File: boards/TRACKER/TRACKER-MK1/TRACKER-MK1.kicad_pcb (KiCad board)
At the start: 2 copper layers, 76.2 x 152.4 mm, 120 parts, among them J101 1054500101, J102 JST-PH, J103 1040310811, J104 JST-PH, J105 JST-PH, J106 JST-PH, J107 JST-PH, J108 JST-PH, J109 JST-PH, J110 U.FL, J111 2.54mm Pin Header, J112 2.54mm Pin Header, J113 2.54mm Pin Header, J114 2.54mm Pin Header, J115 2.54mm Pin Header, J116 2.54mm Pin Header, J117 2.54mm Pin Header, J118 2.54mm Pin Header, J119 2.54mm Pin Header, J120 2.54mm Pin Header, SW101 VBUS Switch, SW102 Battery Switch, SW103 Power Switch, SW104 SW_Push, SW105 SW_Push, U101 BQ25180, U102 ECMF02-2AMX6, U103 ADS7138-Q1, U104 ADS7138-Q1, U105 TPS566242DRLR, U106 ESP32-S3-WROOM-1, U107 BNO085, U108 SAM-M10Q-00B, U201 CC1125, X201 ECS-TXO-2016MV-400-TR

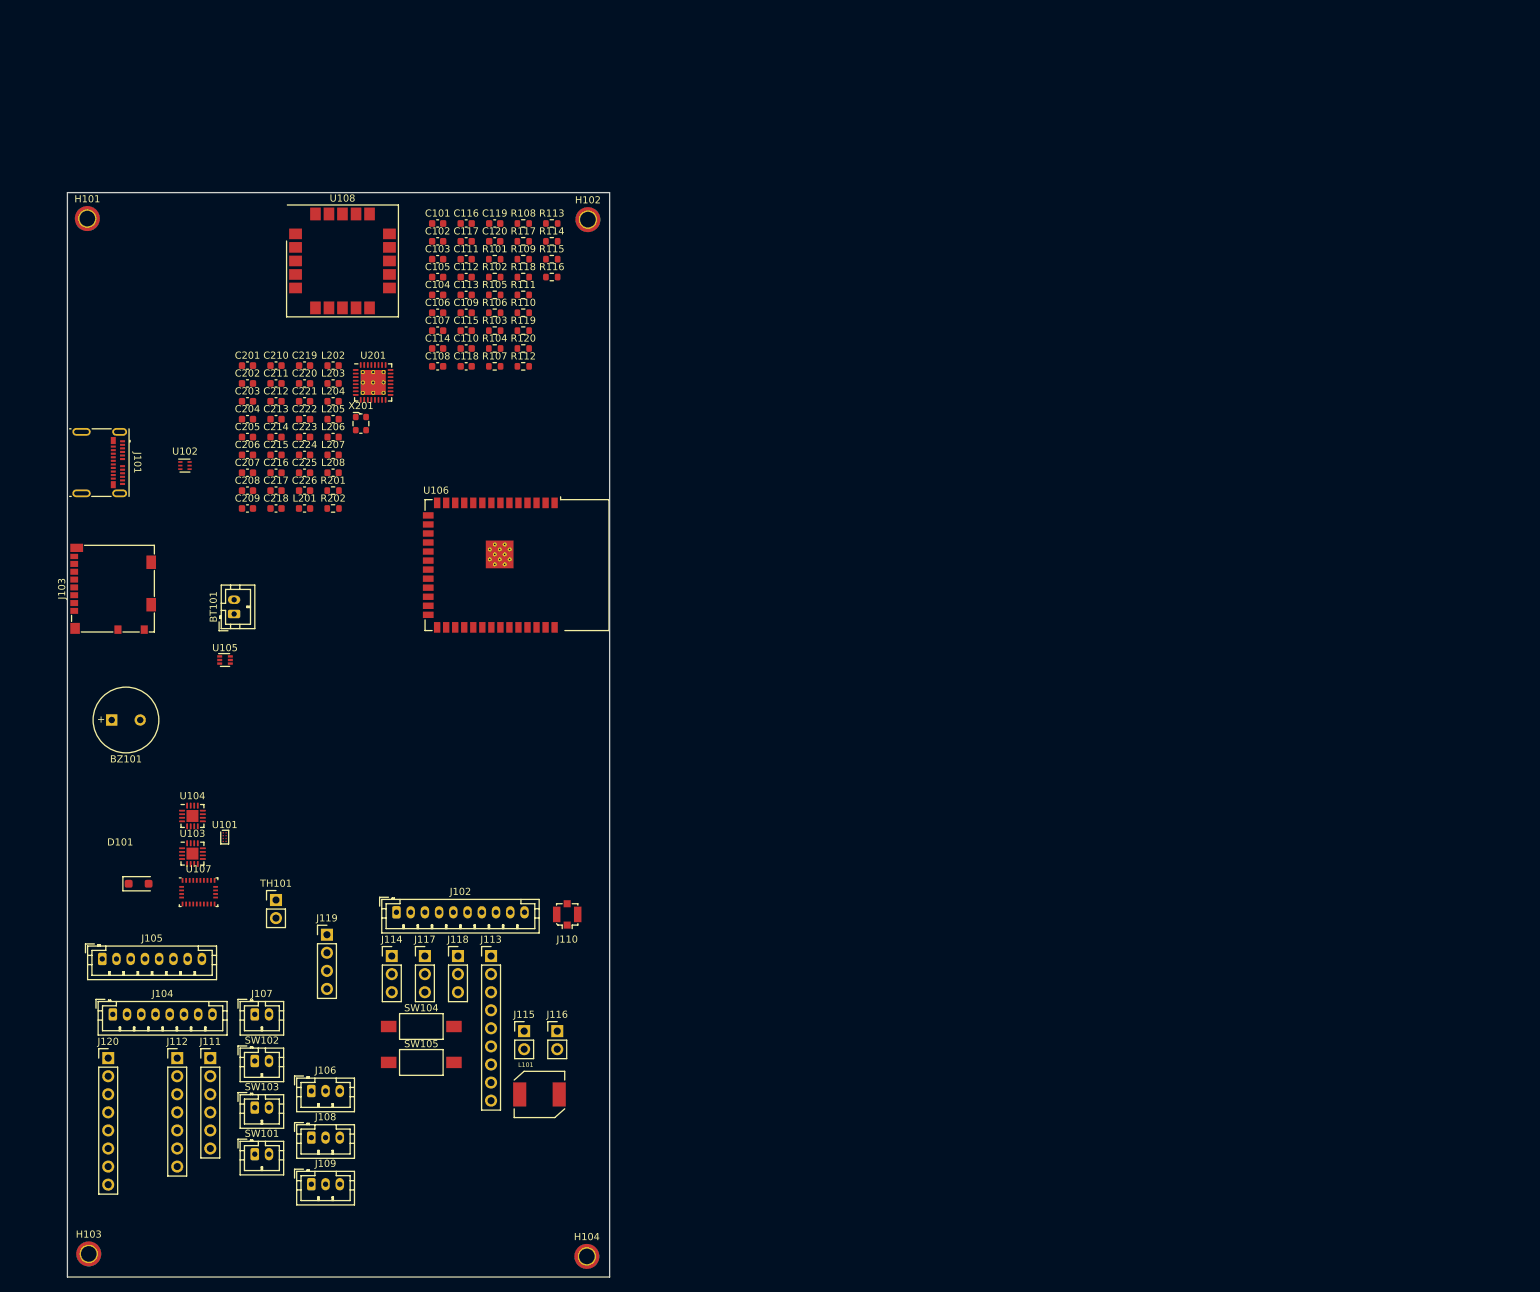
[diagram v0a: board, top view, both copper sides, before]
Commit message: Added GPIO expanders, Done schematic
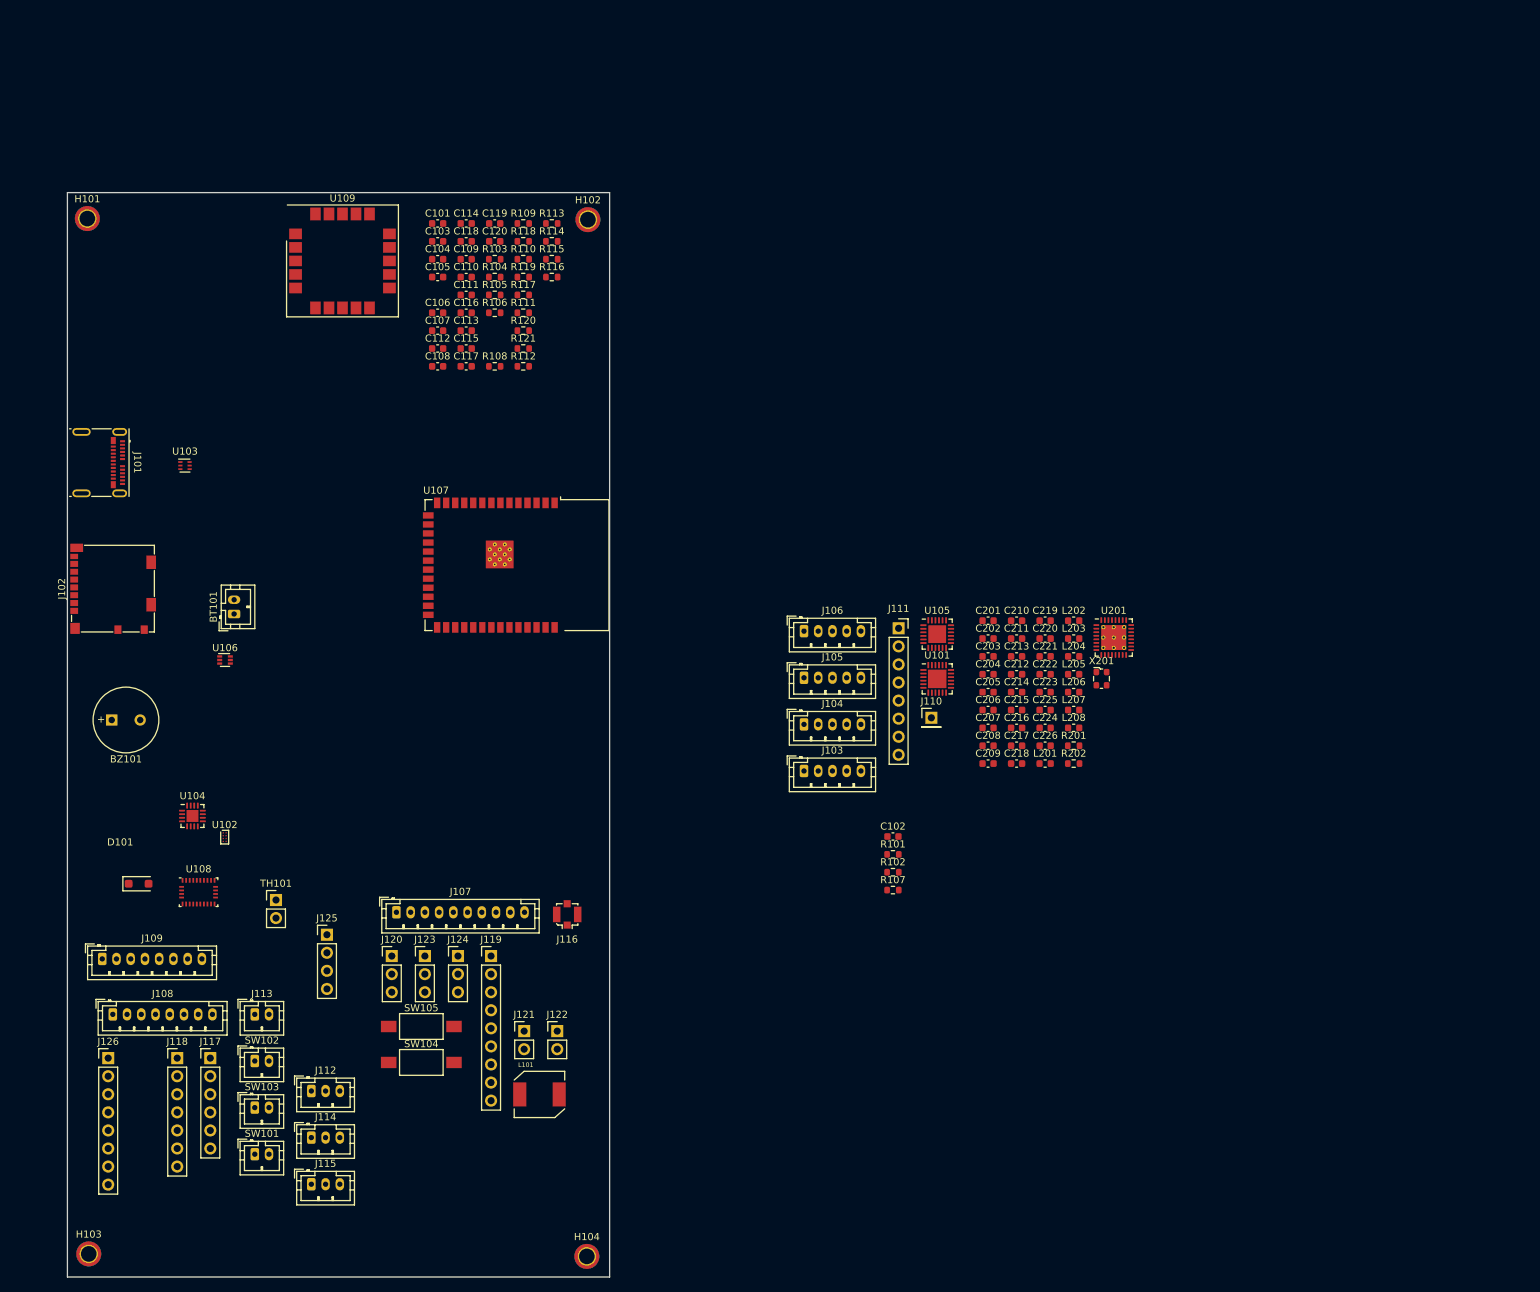
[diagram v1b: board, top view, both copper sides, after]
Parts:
- removed the C104 at (128.2, 39.8)
- removed the R103 at (136.3, 44.8)
- removed the R104 at (136.3, 47.3)
- removed the U103 at (93.8, 118.3)
- added C102: 0.1uF, Capacitor_SMD:C_0603_1608Metric, F.Cu at (192.2, 115.9)
- added J103: JST-PH, Connector_JST:JST_PH_B5B-PH-K_1x05_P2.00mm_Vertical, F.Cu at (179.7, 106.7)
- added J104: JST-PH, Connector_JST:JST_PH_B5B-PH-K_1x05_P2.00mm_Vertical, F.Cu at (179.7, 100.1)
- added J105: JST-PH, Connector_JST:JST_PH_B5B-PH-K_1x05_P2.00mm_Vertical, F.Cu at (179.7, 93.6)
- added J106: JST-PH, Connector_JST:JST_PH_B5B-PH-K_1x05_P2.00mm_Vertical, F.Cu at (179.7, 87.0)
- added J110: 2.54mm Pin Header, Connector_PinHeader_2.54mm:PinHeader_1x01_P2.54mm_Vertical, F.Cu at (197.6, 99.2)
- added J111: 2.54mm Pin Header, Connector_PinSocket_2.54mm:PinSocket_1x08_P2.54mm_Vertical, F.Cu at (193.0, 86.6)
- added R101: 10k, Resistor_SMD:R_0603_1608Metric, F.Cu at (192.2, 118.4)
- added R102: 10k, Resistor_SMD:R_0603_1608Metric, F.Cu at (192.2, 120.9)
- added R107: 10k, Resistor_SMD:R_0603_1608Metric, F.Cu at (192.2, 123.4)
- added U101: TCAL9539-Q1, Package_DFN_QFN:WQFN-24-1EP_4x4mm_P0.5mm_EP2.6x2.6mm, F.Cu at (198.4, 93.7)
- added U105: ADP5589, Package_CSP:LFCSP-24-1EP_4x4mm_P0.5mm_EP2.5x2.5mm, F.Cu at (198.4, 87.5)
- C205: value 47nF -> 33pF
- C206: value 220nF -> 100pF
- C207: value 47nF -> 15pF
- C209: value 33pF -> 220nF
- C210: value 100pF -> 47nF
- C211: value 10nF -> 47nF
- C212: value 47nF -> 3.3pF
- C213: value 47nF -> 1pF
- C214: value 3.3pF -> 47nF
- C215: value 15pF -> 47nF
- C216: value 47nF -> 2.2pF
- C217: value 3.3pF -> 10nF
- C219: value 1pF -> 47nF
- C221: value 47nF -> 3pF
- C222: value 2.2pF -> 3.3pF
- C225: value 3pF -> TBD
- C226: value C -> 47nF
- L202: value 15nH -> 12nH
- L203: value 12nH -> 7.5nH
- L204: value 12nH -> 15nH
- L205: value 7.5nH -> 12nH
- L206: value 12nH -> 18nH
- L207: value 18nH -> 12nH
- moved C212 110.9 mm to (209.6, 93.1)
- moved C224 110.9 mm to (213.6, 100.6)
- moved C207 110.1 mm to (205.6, 100.6)
- moved L208 110.1 mm to (217.6, 100.6)
- moved C210 110.1 mm to (209.6, 85.6)
- moved C215 110.1 mm to (209.6, 98.1)
- moved C216 110.1 mm to (209.6, 100.6)
- moved U201 110.1 mm to (223.2, 87.9)
- moved C201 110.1 mm to (205.6, 85.6)
- moved C202 110.1 mm to (205.6, 88.1)
- moved C203 110.1 mm to (205.6, 90.6)
- moved C204 110.1 mm to (205.6, 93.1)
- moved C205 110.1 mm to (205.6, 95.6)
- moved C206 110.1 mm to (205.6, 98.1)
- moved C208 110.1 mm to (205.6, 103.1)
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- renumbered C102 to C103, C103 to C104, C111 to C109, C112 to C110, C113 to C111, C114 to C112, C115 to C113, C116 to C114, C110 to C115, C109 to C116, C118 to C117, C117 to C118, J103 to J102, J102 to J107, J104 to J108, J105 to J109, J106 to J112, J107 to J113, J108 to J114, J109 to J115, J110 to J116, J111 to J117, J112 to J118, J113 to J119, J114 to J120, J115 to J121, J116 to J122, J117 to J123, J118 to J124, J119 to J125, J120 to J126, R101 to R103, R102 to R104, R107 to R108, R108 to R109, R109 to R110, R110 to R111, R111 to R117, R117 to R118, R118 to R119, R119 to R120, R120 to R121, SW105 to SW104, SW104 to SW105, U101 to U102, U102 to U103, U105 to U106, U106 to U107, U107 to U108, U108 to U109
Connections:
- C204 pad 1: Net-(C204-Pad1) -> /3V3
- C205 pad 1: /3V3 -> Net-(C205-Pad1)
- C205 pad 2: GND -> /3V3
- C206 pad 1: Net-(U201-DCPL) -> /3V3
- C207 pad 1: Net-(U201-DCPL_PFD_CHP) -> Net-(U201-PA)
- C207 pad 2: GND -> Net-(C207-Pad2)
- C209 pad 1: Net-(C209-Pad1) -> Net-(U201-DCPL)
- C209 pad 2: Net-(C204-Pad1) -> GND
- C210 pad 1: Net-(C204-Pad1) -> Net-(U201-DCPL_PFD_CHP)
- C211 pad 1: Net-(U201-DCPL_VCO) -> /3V3
- C212 pad 1: /Radio/DCPL_XOSC -> Net-(C212-Pad1)
- C212 pad 2: GND -> Net-(U201-LNA_N)
- C213 pad 1: /3V3 -> Net-(C207-Pad2)
- C213 pad 2: GND -> Net-(C213-Pad2)
- C214 pad 1: Net-(C214-Pad1) -> /3V3
- C214 pad 2: Net-(U201-LNA_N) -> GND
- C215 pad 1: Net-(U201-PA) -> /3V3
- C215 pad 2: Net-(C215-Pad2) -> GND
- C216 pad 1: /3V3 -> Net-(C213-Pad2)
- C216 pad 2: GND -> Net-(U201-TRX_SW)
- C217 pad 1: GND -> Net-(U201-DCPL_VCO)
- C217 pad 2: Net-(U201-LNA_P) -> GND
- C218 pad 1: /3V3 -> Net-(U201-DCPL_XOSC)
- C219 pad 1: Net-(C215-Pad2) -> /3V3
- C219 pad 2: Net-(C219-Pad2) -> GND
- C221 pad 1: /3V3 -> GND
- C221 pad 2: GND -> Net-(C221-Pad2)
- C222 pad 1: Net-(C219-Pad2) -> GND
- C222 pad 2: Net-(U201-TRX_SW) -> Net-(U201-LNA_P)
- C225 pad 1: GND -> Net-(C221-Pad2)
- C225 pad 2: Net-(C225-Pad2) -> /Radio/ANT
- C226 pad 1: Net-(C225-Pad2) -> /3V3
- C226 pad 2: /Radio/ANT -> GND
- L201 pad 2: Net-(C209-Pad1) -> Net-(C205-Pad1)
- L202 pad 1: Net-(U201-LNA_P) -> GND
- L203 pad 1: Net-(U201-LNA_P) -> Net-(C207-Pad2)
- L203 pad 2: Net-(C214-Pad1) -> Net-(C213-Pad2)
- L204 pad 2: GND -> Net-(U201-LNA_P)
- L205 pad 1: Net-(C215-Pad2) -> Net-(U201-TRX_SW)
- L205 pad 2: Net-(C219-Pad2) -> Net-(C212-Pad1)
- L206 pad 1: Net-(C214-Pad1) -> Net-(C213-Pad2)
- L206 pad 2: Net-(U201-TRX_SW) -> Net-(C221-Pad2)
- L207 pad 1: Net-(C219-Pad2) -> Net-(C212-Pad1)
- L207 pad 2: Net-(C225-Pad2) -> Net-(U201-LNA_P)
- L208 pad 1: Net-(C225-Pad2) -> Net-(C221-Pad2)
- R202 pad 1: Net-(C209-Pad1) -> Net-(C205-Pad1)
- R202 pad 2: Net-(C204-Pad1) -> /3V3
- U107 pad 10: / DISPLAY_CS -> /SD_DAT3
- U107 pad 11: / DISPLAY_SCLK -> / DISPLAY_CS
- U107 pad 12: / DISPLAY_MOSI -> / DISPLAY_SCLK
- U107 pad 13: /USB_ESP_DN -> / DISPLAY_MOSI
- U107 pad 14: /USB_ESP_DP -> /USB_ESP_DN
- U107 pad 15: unconnected-(U106-IO3-Pad15) -> /USB_ESP_DP
- U107 pad 16: GND -> unconnected-(U107-IO46-Pad16)
- U107 pad 17: /PWM_BUZZER -> GND
- U107 pad 3: /CHIP_PU -> unconnected-(U107-EN-Pad3)
- U107 pad 35: /BQ25180_INT -> /PWM_BUZZER
- U107 pad 36: /ADC1_ALERT -> /ADP_~{RESET}
- U107 pad 37: /ADC0_ALERT -> /ADP_~{INT}
- U107 pad 4: /SD_CLK -> /CHIP_PU
- U107 pad 5: /SD_CMD -> /SD_CLK
- U107 pad 6: /SD_DAT1 -> /SD_CMD
- U107 pad 7: /SD_DAT0 -> /SD_DAT1
- U107 pad 8: /SD_DAT2 -> /SD_DAT0
- U107 pad 9: /SD_DAT3 -> /SD_DAT2
- U201 pad 29: /Radio/DCPL_XOSC -> Net-(U201-DCPL_XOSC)

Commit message: Worked on routing
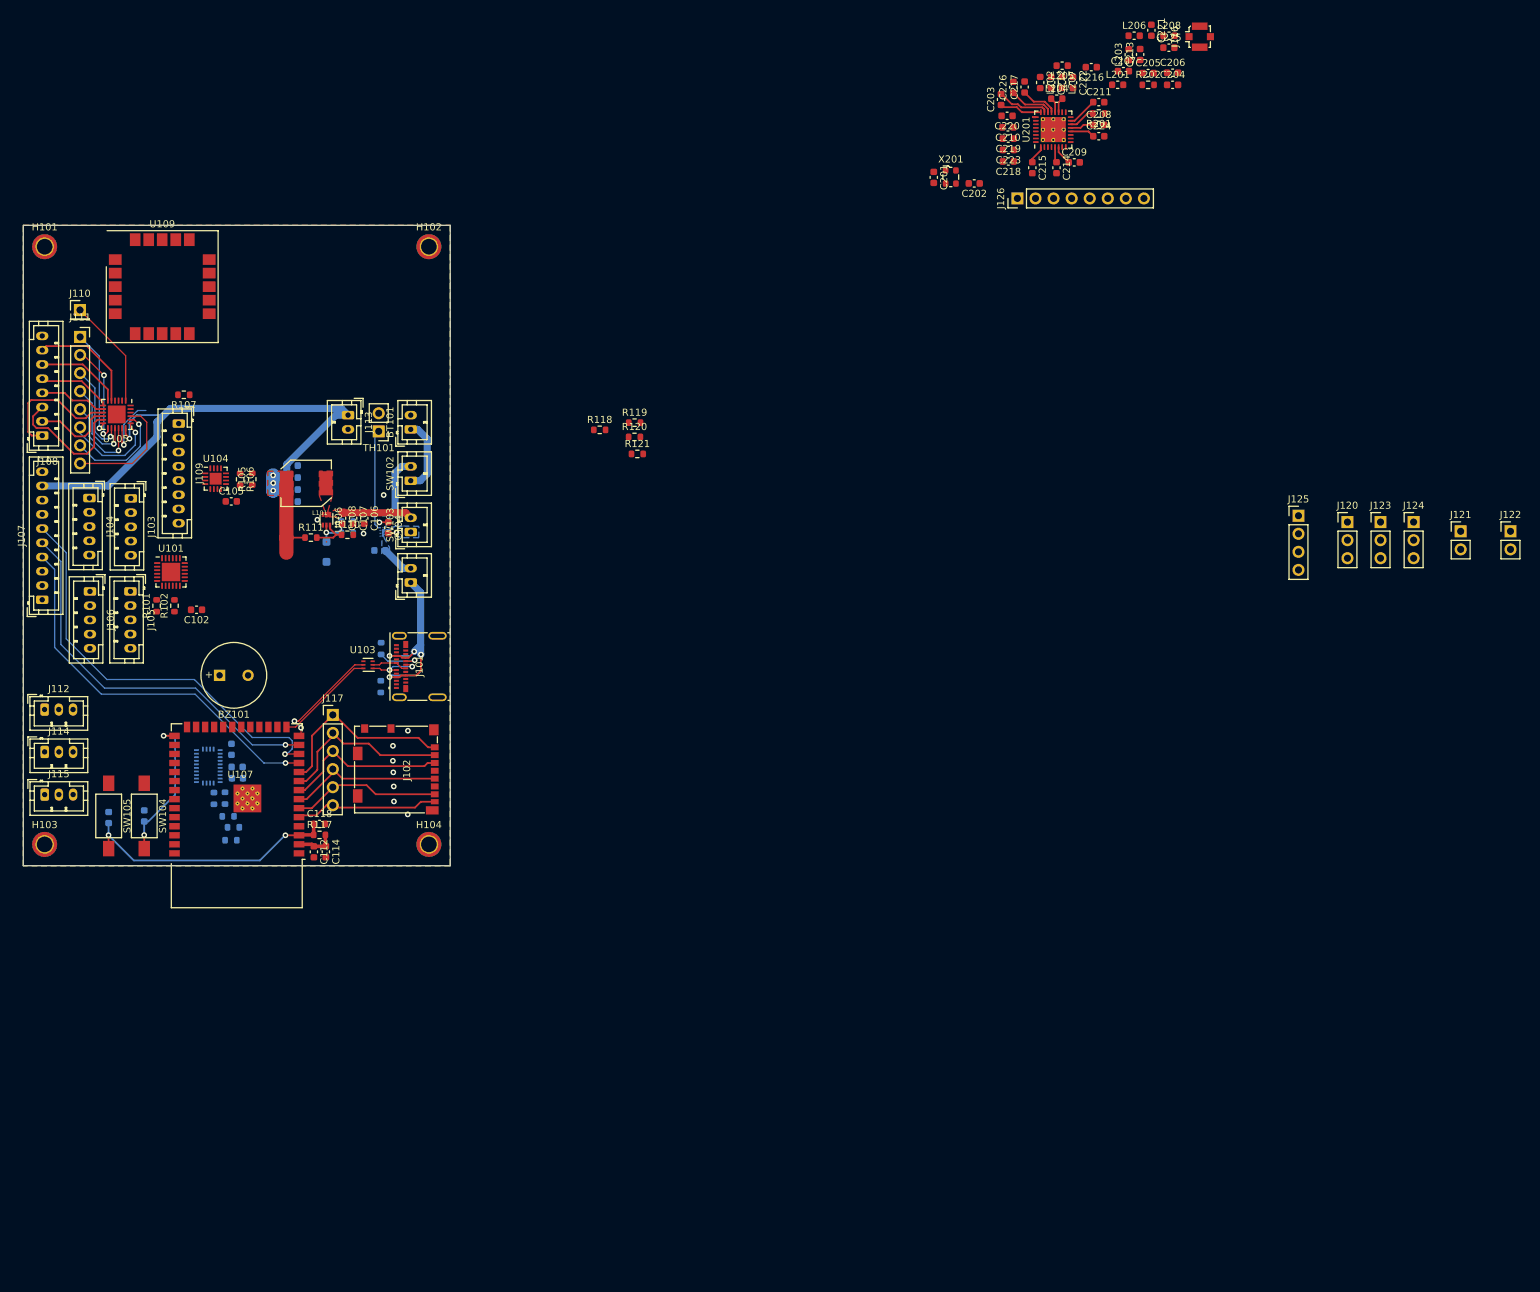
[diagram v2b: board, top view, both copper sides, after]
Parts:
- removed J118: 2.54mm Pin Header, Connector_PinHeader_2.54mm:PinHeader_1x07_P2.54mm_Vertical
- removed J119: 2.54mm Pin Header, Connector_PinHeader_2.54mm:PinHeader_1x09_P2.54mm_Vertical
- C101, C103, C109, C110, C111, C113, C115, C116, C117, C119, C120, D101, R103, R104, R108, R109, R112, R113, R114, R115, R116, U102, U108: moved to B.Cu
- moved J126 175.9 mm to (209.7, 26.2), turned to 90 degrees
- moved J116 152.0 mm to (235.3, 3.49), turned to -90 degrees
- moved J122 151.3 mm to (279.0, 73.0)
- moved J121 149.2 mm to (272.0, 73.0)
- moved J125 148.7 mm to (249.2, 70.8)
- moved J123 147.5 mm to (260.7, 71.7)
- moved J120 147.5 mm to (256.1, 71.7)
- moved J124 147.5 mm to (265.4, 71.7)
- moved J110 132.7 mm to (78.0, 41.9)
- moved J111 122.1 mm to (78.0, 45.7)
- moved R107 121.6 mm to (92.6, 53.8), turned to 180 degrees
- moved U105 119.4 mm to (83.1, 56.6), turned to -90 degrees
- moved R101 109.2 mm to (88.7, 83.5), turned to 90 degrees
- moved U101 108.7 mm to (90.8, 78.7)
- moved R102 107.7 mm to (91.2, 83.5), turned to 90 degrees
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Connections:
- net Net-(U103-D+_in) renamed /DP
- net Net-(U103-D-_in) renamed /DN
- U107 pad 10: /SD_DAT3 -> /SD_DAT2
- U107 pad 3: unconnected-(U107-EN-Pad3) -> /CHIP_PU
- U107 pad 4: /CHIP_PU -> unconnected-(U107-IO4-Pad4)
- U107 pad 5: /SD_CLK -> /SD_DAT1
- U107 pad 6: /SD_CMD -> /SD_DAT0
- U107 pad 7: /SD_DAT1 -> /SD_CLK
- U107 pad 8: /SD_DAT0 -> /SD_CMD
- U107 pad 9: /SD_DAT2 -> /SD_DAT3
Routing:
- net /3V3: track 0.00 -> 125.4 mm, vias 0 -> 4
- net / DISPLAY_SCLK: track 0.00 -> 59.1 mm, vias 0 -> 1
- net / DISPLAY_MOSI: track 0.00 -> 54.7 mm, vias 0 -> 1
- net / DISPLAY_CS: track 0.00 -> 54.5 mm, vias 0 -> 1
- net /CHIP_PU: track 0.00 -> 37.0 mm, vias 0 -> 2
- net Net-(SW101-A): track 0.00 -> 34.7 mm, vias 0 -> 4
- net /SD_DAT2: track 0.00 -> 26.8 mm
- net /SD_DAT3: track 0.00 -> 24.9 mm
- net /SD_CMD: track 0.00 -> 23.3 mm
- net /SD_CLK: track 0.00 -> 21.7 mm
- net /GPIO_0: track 0.00 -> 21.1 mm, vias 0 -> 2
- net /SD_DAT0: track 0.00 -> 20.9 mm
- net /SD_DAT1: track 0.00 -> 20.2 mm
- net /KEYPAD_C3: track 0.00 -> 18.4 mm
- net /KEYPAD_C1: track 0.00 -> 18.3 mm
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- added copper zone on F.Cu, net /3V3
- added copper zone on B.Cu, net /VBAT
- added copper zone on B.Cu, net /VBUS
- added copper zone on F.Cu, net /VSYS
- added copper zone on B.Cu, net GND
- added copper zone on F.Cu, net GND
- added copper zone on B.Cu, net Net-(SW103-A)
- added copper zone on F.Cu, net Net-(U106-SW)
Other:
- board size 76.2 x 152.4 mm -> 60 x 90 mm
